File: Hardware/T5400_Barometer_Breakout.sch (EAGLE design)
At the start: 11 parts, among them U1 T5400

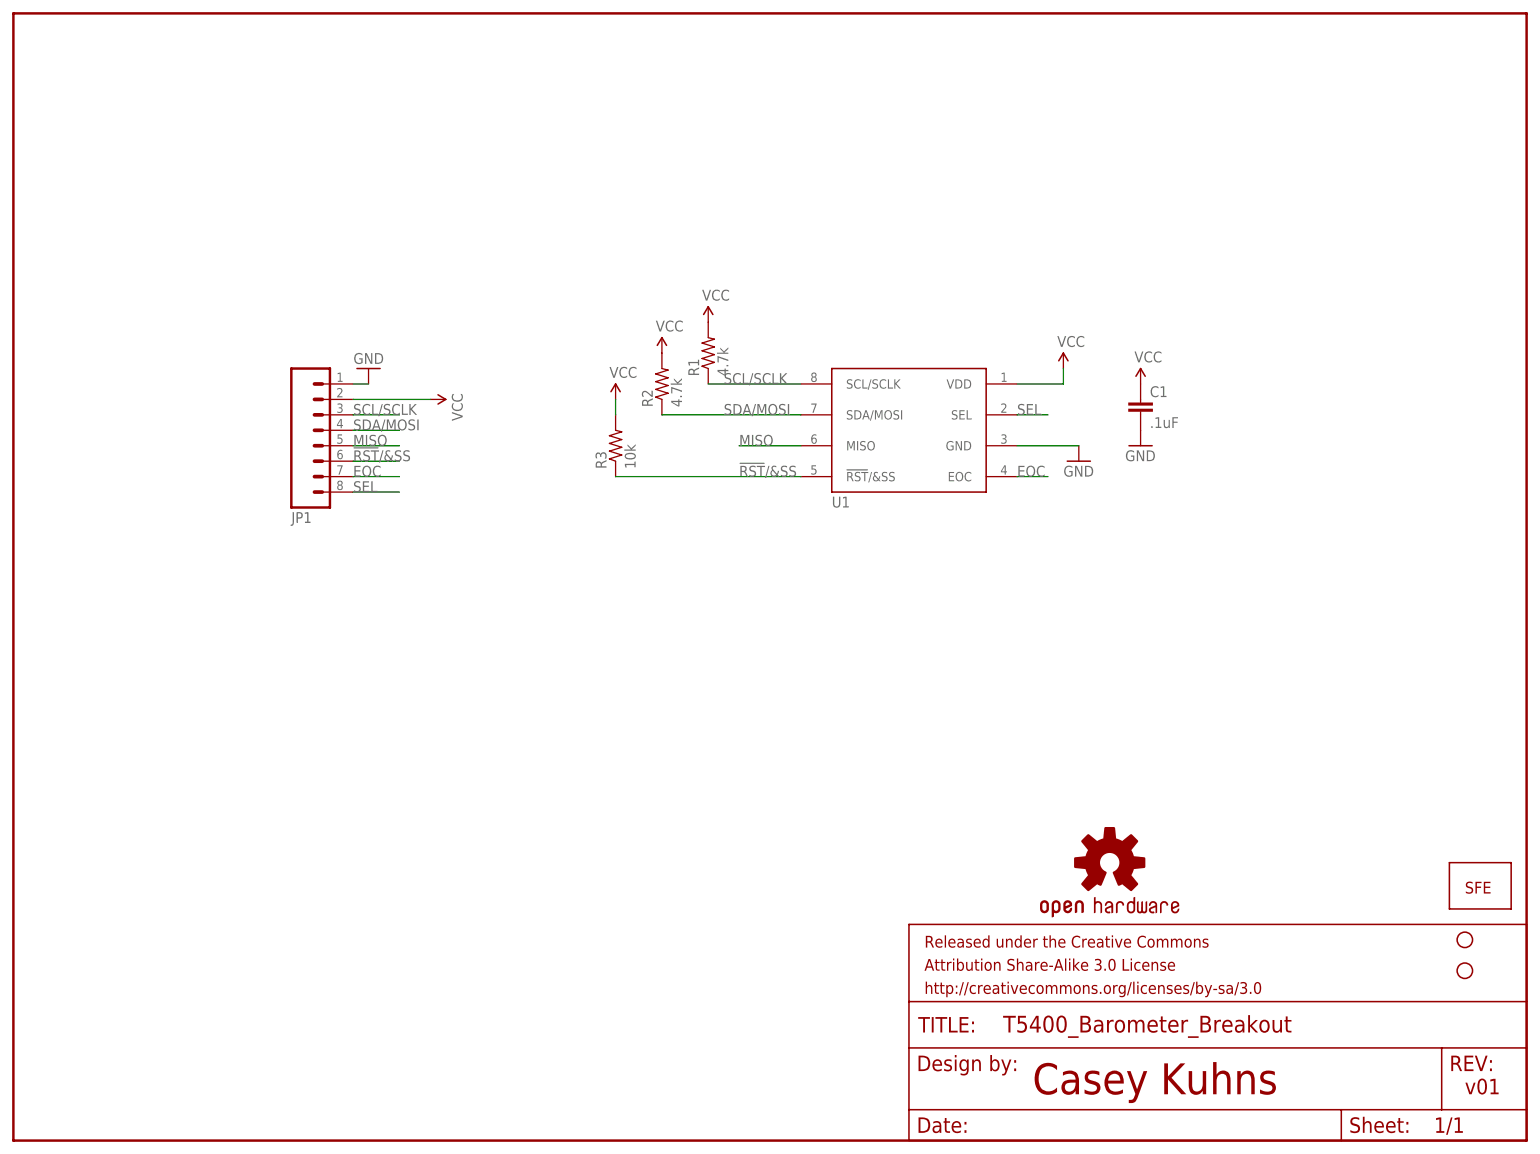
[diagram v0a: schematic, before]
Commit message: READY for proto
Corrected boards per meeting agenda.  Also changed names
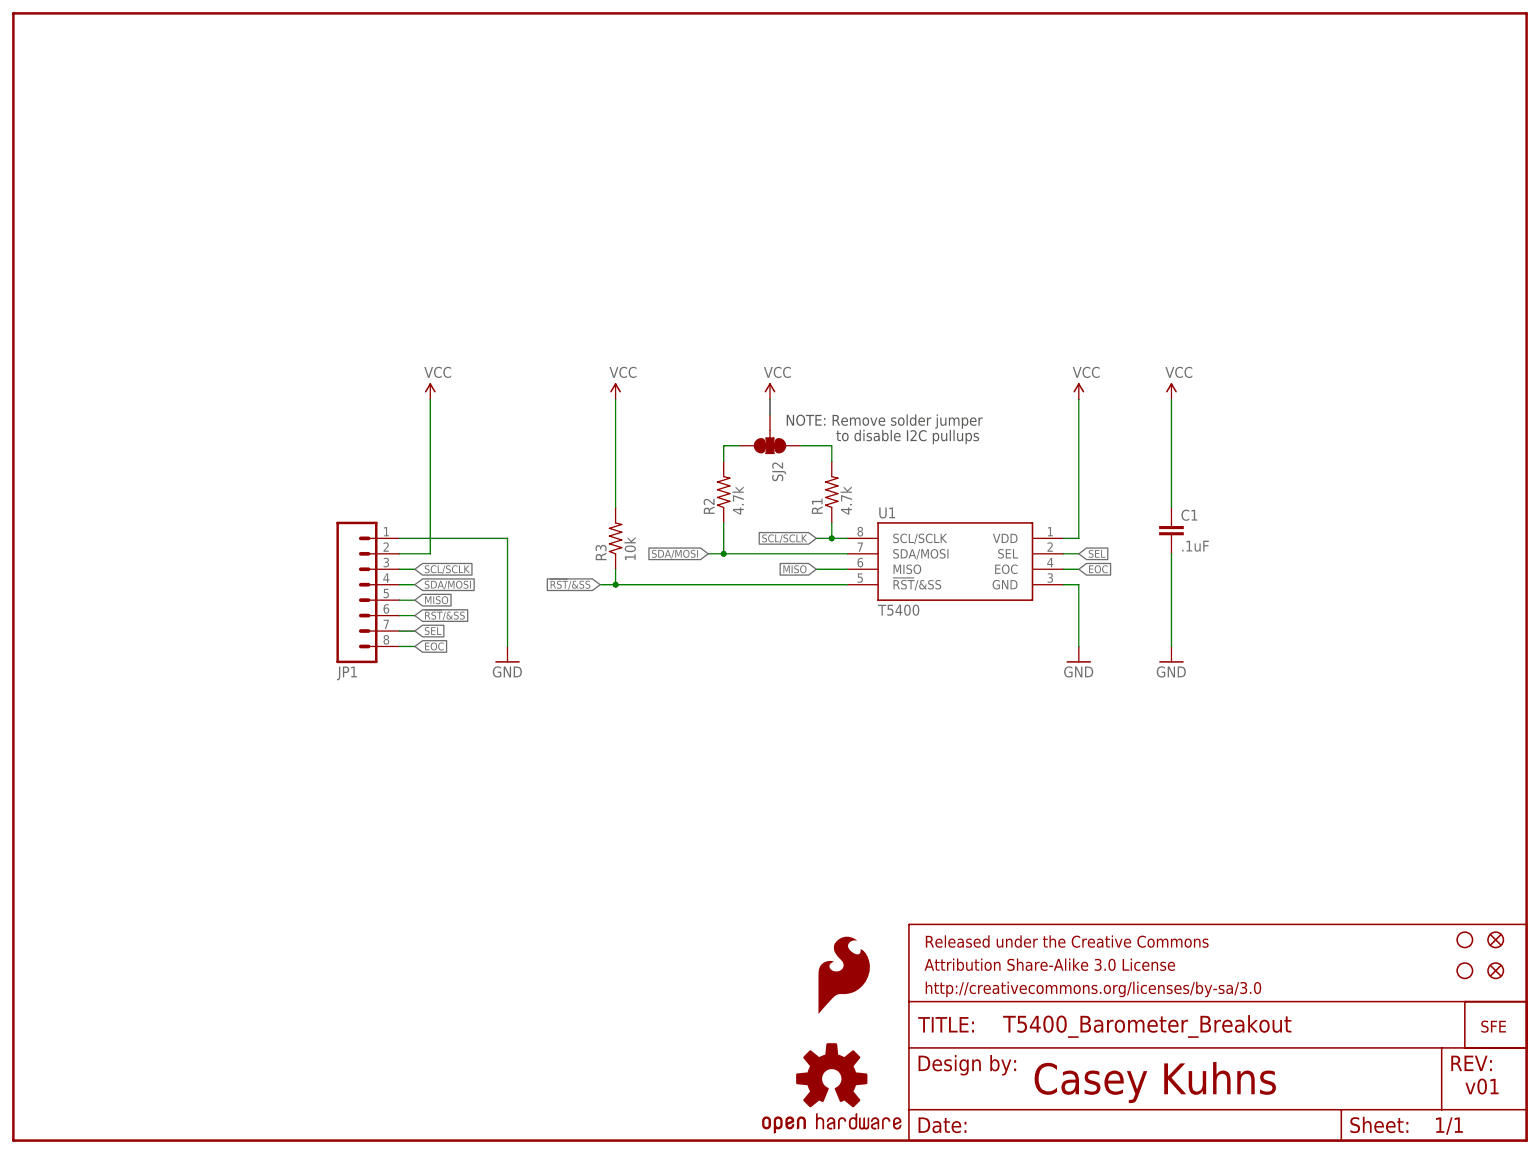
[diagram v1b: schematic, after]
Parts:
- added FID1, FID2: FIDUCIAL1X2, SparkFun-Aesthetics:FIDUCIAL1X2
- added LOGO3: SFE_LOGO_FLAME.1_INCH, SparkFun-Aesthetics:SFE_LOGO_FLAME.1_INCH
- added SJ2: (no value), SparkFun-Passives:SOLDERJUMPER_2WAYPASTE1&2&3
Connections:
- new net N$1: R2.2, SJ2.3
- new net N$2: R1.2, SJ2.1
- net EOC: now also JP1.8; no longer JP1.7
- net SEL: now also JP1.7; no longer JP1.8
- net VCC: now also SJ2.2; no longer R1.2, R2.2
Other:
- note added: "NOTE: Remove solder jumper"
- note added: "to disable I2C pullups"
- moved on the sheet: C1, JP1, R1, R2, R3, U1

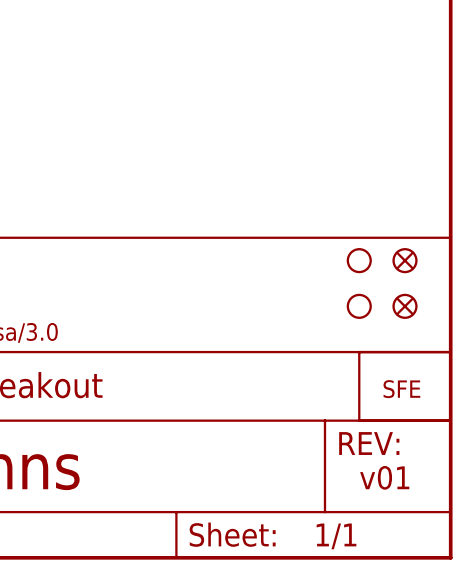
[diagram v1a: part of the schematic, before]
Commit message: removed fiducials
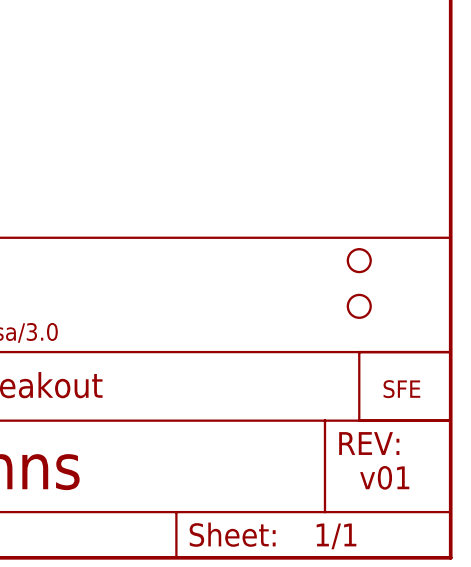
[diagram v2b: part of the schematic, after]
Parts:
- removed FID1, FID2: FIDUCIAL1X2, SparkFun-Aesthetics:FIDUCIAL1X2
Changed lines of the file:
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@@
 <?xml version="1.0" encoding="utf-8"?>
 <!DOCTYPE eagle SYSTEM "eagle.dtd">
-<eagle version="6.0">
+<eagle version="6.5.0">
 <drawing>
 <settings>
@@
 <part name="R3" library="SparkFun-Passives" deviceset="RESISTOR" device="0603-RES" value="10k"/>
 <part name="SUPPLY6" library="SparkFun-Aesthetics" deviceset="VCC" device=""/>
-<part name="FID1" library="SparkFun-Aesthetics" deviceset="FIDUCIAL" device="1X2"/>
-<part name="FID2" library="SparkFun-Aesthetics" deviceset="FIDUCIAL" device="1X2"/>
 <part name="LOGO3" library="SparkFun-Aesthetics" deviceset="SFE_LOGO_FLAME" device=".1_INCH"/>
 <part name="SJ2" library="SparkFun-Passives" deviceset="SOLDERJUMPER_2WAY" device="PASTE1&amp;2&amp;3"/>
@@
 <instance part="R3" gate="G$1" x="99.06" y="99.06" rot="R90"/>
 <instance part="SUPPLY6" gate="1" x="99.06" y="121.92"/>
-<instance part="FID1" gate="G$1" x="243.84" y="27.94"/>
-<instance part="FID2" gate="G$1" x="243.84" y="33.02"/>
 <instance part="LOGO3" gate="G$1" x="132.08" y="20.32"/>
 <instance part="SJ2" gate="G$1" x="124.46" y="114.3" rot="R270"/>
